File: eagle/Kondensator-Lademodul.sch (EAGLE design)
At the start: 24 parts, among them IC3 7818TV, X1 MKDSN1,5/2-5,08, X2 MKDSN1,5/2-5,08, X3 MKDSN1,5/2-5,08

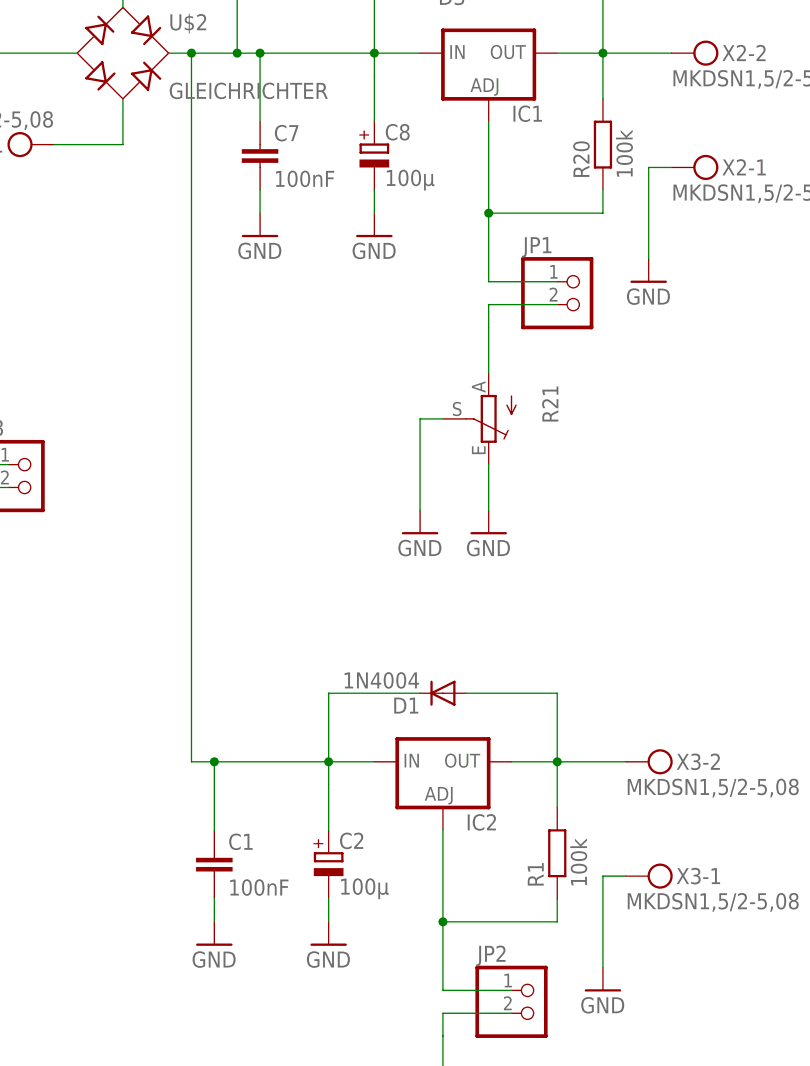
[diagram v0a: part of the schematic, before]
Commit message: Fixed setup of capacitors (bigger and not in conflict)
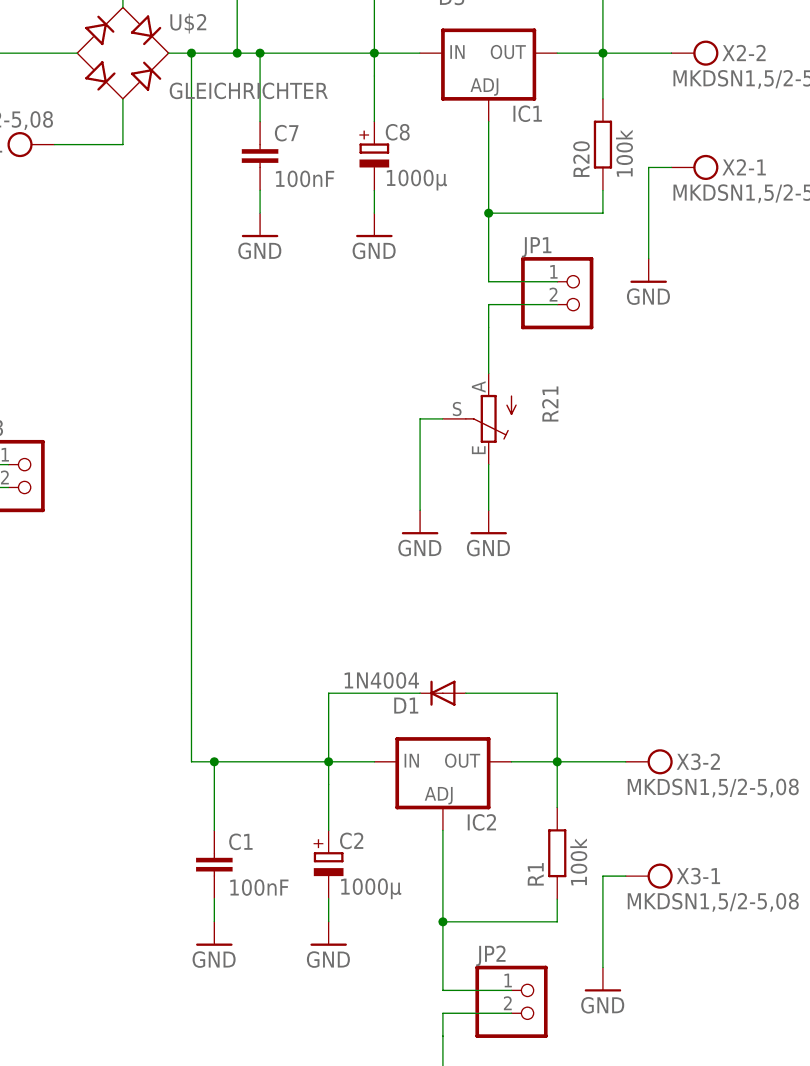
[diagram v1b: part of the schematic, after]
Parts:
- C2, C8: value 100µ -> 1000µ; device rcl:CPOL-EUE3.5-8 -> rcl:CPOL-EUE5-13
- C4: device rcl:CPOL-EUE3.5-8 -> rcl:CPOL-EUE5-13
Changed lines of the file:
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@@
 <part name="X1" library="con-phoenix-508" deviceset="MKDSN1,5/2-5,08" device=""/>
 <part name="C7" library="rcl" deviceset="C-EU" device="C0805" value="100nF"/>
-<part name="C8" library="rcl" deviceset="CPOL-EU" device="E3.5-8" value="100µ"/>
+<part name="C8" library="rcl" deviceset="CPOL-EU" device="E5-13" value="1000µ"/>
 <part name="D3" library="diode" deviceset="1N4004" device=""/>
 <part name="R20" library="rcl" deviceset="R-EU_" device="R1206" value="100k"/>
@@
 <part name="IC2" library="v-reg" deviceset="LM317TS" device=""/>
 <part name="C1" library="rcl" deviceset="C-EU" device="C0805" value="100nF"/>
-<part name="C2" library="rcl" deviceset="CPOL-EU" device="E3.5-8" value="100µ"/>
+<part name="C2" library="rcl" deviceset="CPOL-EU" device="E5-13" value="1000µ"/>
 <part name="D1" library="diode" deviceset="1N4004" device=""/>
 <part name="R1" library="rcl" deviceset="R-EU_" device="R1206" value="100k"/>
@@
 <part name="GND6" library="supply1" deviceset="GND" device=""/>
 <part name="IC3" library="linear" deviceset="78*" device="TV" technology="05" value="7818TV"/>
-<part name="C4" library="rcl" deviceset="CPOL-EU" device="E3.5-8" value="1000µ"/>
+<part name="C4" library="rcl" deviceset="CPOL-EU" device="E5-13" value="1000µ"/>
 <part name="C5" library="rcl" deviceset="C-EU" device="C0805" value="100nF"/>
 <part name="GND10" library="supply1" deviceset="GND" device=""/>

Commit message: Var. Changes. Layout and new diode for 7818
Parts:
- added D2: 1N4004, diode:1N4004
- added JP5: (no value), pinhead:PINHD-1X2
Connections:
- net N$17: now also D2.C
- net N$2: now also D2.A, JP5.1
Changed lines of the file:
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@@
 <part name="GND7" library="supply1" deviceset="GND" device=""/>
 <part name="JP4" library="pinhead" deviceset="PINHD-1X2" device=""/>
+<part name="D2" library="diode" deviceset="1N4004" device=""/>
+<part name="JP5" library="pinhead" deviceset="PINHD-1X2" device=""/>
 </parts>
 <sheets>
@@
 <instance part="GND7" gate="1" x="17.78" y="53.34"/>
 <instance part="JP4" gate="G$1" x="30.48" y="71.12"/>
+<instance part="D2" gate="1" x="-2.54" y="86.36" rot="R180"/>
+<instance part="JP5" gate="G$1" x="43.18" y="71.12"/>
 </instances>
 <busses>
@@
 <wire x1="-40.64" y1="73.66" x2="-40.64" y2="30.48" width="0.1524" layer="91"/>
 <junction x="-40.64" y="30.48"/>
+<pinref part="D2" gate="1" pin="C"/>
+<wire x1="-5.08" y1="86.36" x2="-25.4" y2="86.36" width="0.1524" layer="91"/>
+<wire x1="-25.4" y1="86.36" x2="-25.4" y2="73.66" width="0.1524" layer="91"/>
 </segment>
 </net>
@@
 <junction x="10.16" y="73.66"/>
 <pinref part="JP4" gate="G$1" pin="1"/>
-</segment>
-</net>
+<wire x1="10.16" y1="73.66" x2="10.16" y2="86.36" width="0.1524" layer="91"/>
+<pinref part="D2" gate="1" pin="A"/>
+<wire x1="10.16" y1="86.36" x2="0" y2="86.36" width="0.1524" layer="91"/>
+<pinref part="JP5" gate="G$1" pin="1"/>
+<wire x1="27.94" y1="73.66" x2="40.64" y2="73.66" width="0.1524" layer="91"/>
+<junction x="27.94" y="73.66"/>
+</segment>
+</net>

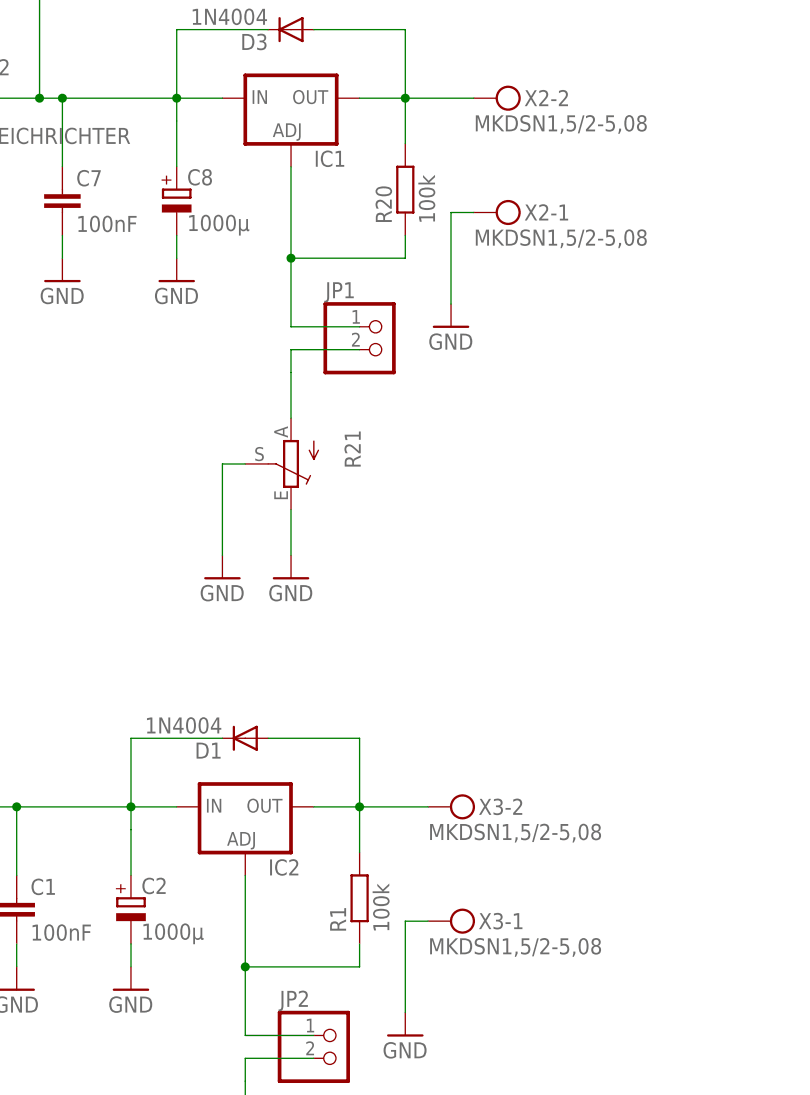
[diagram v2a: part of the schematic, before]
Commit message: Updated wrong resistor value
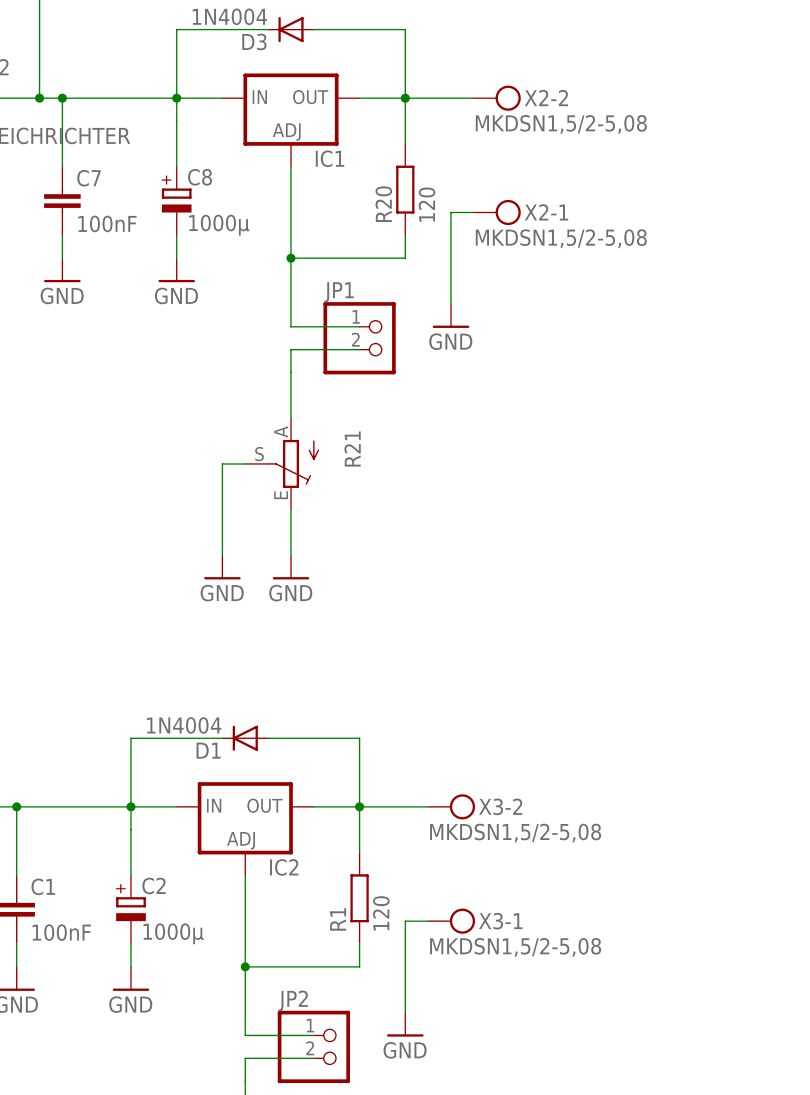
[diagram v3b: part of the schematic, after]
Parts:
- R1, R20: value 100k -> 120
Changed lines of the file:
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@@
 <part name="C8" library="rcl" deviceset="CPOL-EU" device="E5-13" value="1000µ"/>
 <part name="D3" library="diode" deviceset="1N4004" device=""/>
-<part name="R20" library="rcl" deviceset="R-EU_" device="R1206" value="100k"/>
+<part name="R20" library="rcl" deviceset="R-EU_" device="R1206" value="120"/>
 <part name="R21" library="pot" deviceset="TRIM_EU-" device="PT10"/>
 <part name="JP1" library="pinhead" deviceset="PINHD-1X2" device=""/>
@@
 <part name="C2" library="rcl" deviceset="CPOL-EU" device="E5-13" value="1000µ"/>
 <part name="D1" library="diode" deviceset="1N4004" device=""/>
-<part name="R1" library="rcl" deviceset="R-EU_" device="R1206" value="100k"/>
+<part name="R1" library="rcl" deviceset="R-EU_" device="R1206" value="120"/>
 <part name="R2" library="pot" deviceset="TRIM_EU-" device="PT10"/>
 <part name="JP2" library="pinhead" deviceset="PINHD-1X2" device=""/>
